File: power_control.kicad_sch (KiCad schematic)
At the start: 21 parts, among them J3 Conn_01x03_Pin, Q1 2N7002, Q2 2N7002, Q3 DTC143Z, SW1 SW_Slide_DPDT, SW2 SW_Push, U4 TPD1E10B06DPYR, U5 TPD1E10B06DPYR

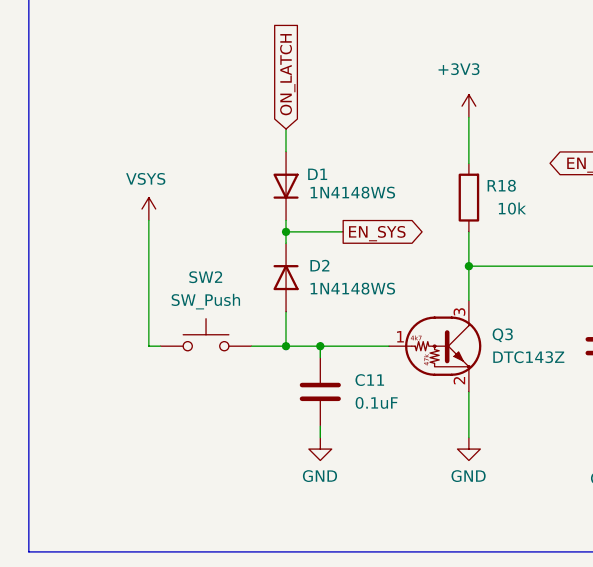
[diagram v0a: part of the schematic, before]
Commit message: v1 Revision - Better routing - Added testpoints - DUCK - Tweaked drawings
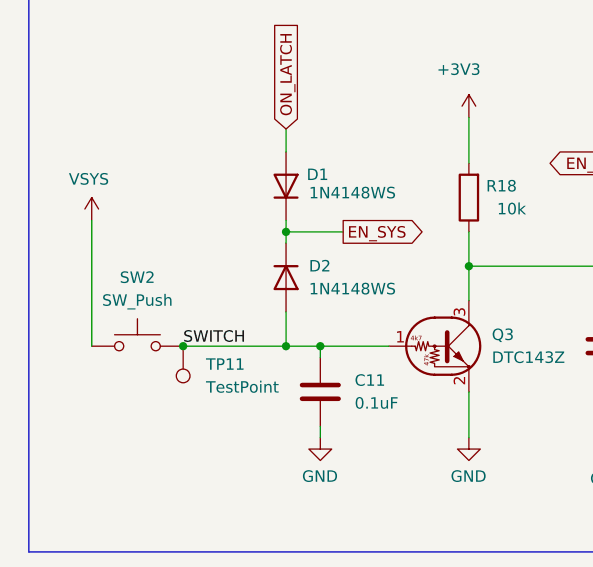
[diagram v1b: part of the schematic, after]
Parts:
- added TP11: TestPoint, TestPoint:TestPoint_Pad_D1.0mm, symbol Connector:TestPoint
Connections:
- net SWITCH: now reaches C11.1, D2.2 (A), Q3.1 (B), SW2.2
- net SWITCH: now also TP11.1
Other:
- moved on the sheet: SW2
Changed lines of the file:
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@@
 	)
 	(junction
+		(at 81.28 144.78)
+		(diameter 0)
+		(color 0 0 0 0)
+	)
+	(junction
 		(at 134.62 124.46)
 		(diameter 0)
@@
 	(wire
 		(pts
-			(xy 88.9 144.78) (xy 92.71 144.78)
+			(xy 81.28 144.78) (xy 92.71 144.78)
 		)
 		(stroke
@@
 	(wire
 		(pts
-			(xy 77.47 130.81) (xy 77.47 144.78)
+			(xy 71.12 130.81) (xy 71.12 144.78)
 		)
 		(stroke
@@
 	(wire
 		(pts
-			(xy 77.47 144.78) (xy 78.74 144.78)
-		)
-		(stroke
-			(width 0)
-			(type default)
-		)
-	)
-	(wire
-		(pts
 			(xy 170.18 86.36) (xy 170.18 88.9)
 		)
@@
 		)
 	)
+	(label "SWITCH"
+		(at 81.28 144.78 0)
+		(effects
+			(font
+				(size 1.27 1.27)
+			)
+			(justify left bottom)
+		)
+	)
 	(global_label "EN_LOAD_BATT"
 		(shape input)
@@
 	)
 	(symbol
+		(lib_id "Connector:TestPoint")
+		(at 81.28 144.78 180)
+		(unit 1)
+		(exclude_from_sim no)
+		(in_bom no)
+		(on_board yes)
+		(dnp no)
+		(fields_autoplaced yes)
+		(property "Reference" "TP11"
+			(at 83.82 146.8119 0)
+			(effects
+				(font
+					(size 1.27 1.27)
+				)
+				(justify right)
+			)
+		)
+		(property "Value" "TestPoint"
+			(at 83.82 149.3519 0)
+			(effects
+				(font
+					(size 1.27 1.27)
+				)
+				(justify right)
+			)
+		)
+		(property "Footprint" "TestPoint:TestPoint_Pad_D1.0mm"
+			(at 76.2 144.78 0)
+			(effects
+				(font
+					(size 1.27 1.27)
+				)
+				(hide yes)
+			)
+		)
+		(property "Datasheet" "~"
+			(at 76.2 144.78 0)
+			(effects
+				(font
+					(size 1.27 1.27)
+				)
+				(hide yes)
+			)
+		)
+		(property "Description" "test point"
+			(at 81.28 144.78 0)
+			(effects
+				(font
+					(size 1.27 1.27)
+				)
+				(hide yes)
+			)
+		)
+		(pin "1"
+		)
+		(instances
+			(project "DRP.004"
+				(path "/990f0ec4-1b5b-4db8-8f39-ecd88fffeea0/6cce2e90-e51c-4942-a042-f4f9f078d271/72eb472c-a375-4523-9048-0cd870109a09"
+					(reference "TP11")
+					(unit 1)
+				)
+			)
+		)
+	)
+	(symbol
 		(lib_id "power:GND")
 		(at 119.38 91.44 0)
@@
 	(symbol
 		(lib_id "power:VCC")
-		(at 77.47 130.81 0)
+		(at 71.12 130.81 0)
 		(mirror y)
 		(unit 1)
@@
 		(dnp no)
 		(property "Reference" "#PWR038"
-			(at 77.47 134.62 0)
+			(at 71.12 134.62 0)
 			(effects
 				(font
@@
 		)
 		(property "Value" "VSYS"
-			(at 74.93 126.238 0)
+			(at 68.58 126.238 0)
 			(effects
 				(font
@@
 		)
 		(property "Footprint" ""
-			(at 77.47 130.81 0)
+			(at 71.12 130.81 0)
 			(effects
 				(font
@@
 		)
 		(property "Datasheet" ""
-			(at 77.47 130.81 0)
+			(at 71.12 130.81 0)
 			(effects
 				(font
@@
 		)
 		(property "Description" "Power symbol creates a global label with name \"VCC\""
-			(at 77.47 130.81 0)
+			(at 71.12 130.81 0)
 			(effects
 				(font
@@
 	(symbol
 		(lib_id "Switch:SW_Push")
-		(at 83.82 144.78 0)
+		(at 76.2 144.78 0)
 		(unit 1)
 		(exclude_from_sim no)
@@
 		(fields_autoplaced yes)
 		(property "Reference" "SW2"
-			(at 83.82 137.16 0)
+			(at 76.2 137.16 0)
 			(effects
 				(font
@@
 		)
 		(property "Value" "SW_Push"
-			(at 83.82 139.7 0)
+			(at 76.2 139.7 0)
 			(effects
 				(font
@@
 		)
 		(property "Footprint" "SWITCHES:SW_SPST_PTS645"
-			(at 83.82 139.7 0)
+			(at 76.2 139.7 0)
 			(effects
 				(font
@@
 		)
 		(property "Datasheet" "~"
-			(at 83.82 139.7 0)
+			(at 76.2 139.7 0)
 			(effects
 				(font
@@
 		)
 		(property "Description" "Push button switch, generic, two pins"
-			(at 83.82 144.78 0)
+			(at 76.2 144.78 0)
 			(effects
 				(font
@@
 		)
 		(property "LCSC" "C2837531"
-			(at 83.82 144.78 0)
+			(at 76.2 144.78 0)
 			(effects
 				(font
@@
 		)
 		(property "lcsc" ""
-			(at 83.82 144.78 0)
+			(at 76.2 144.78 0)
 			(effects
 				(font

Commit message: v2 Rev
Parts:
- removed R14, R15: 100k, Resistor_SMD:R_0603_1608Metric, symbol Device:R
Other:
- moved on the sheet: C15, Q1, R12

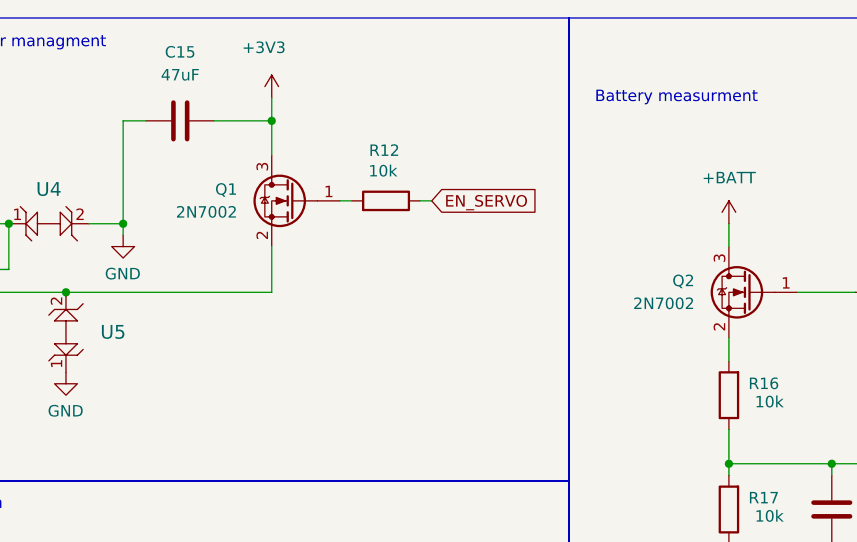
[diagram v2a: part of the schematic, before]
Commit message: Buffed MOSFETs - Changed Q1,Q2 to AO3400 - Changed Q4 to DMG1012T
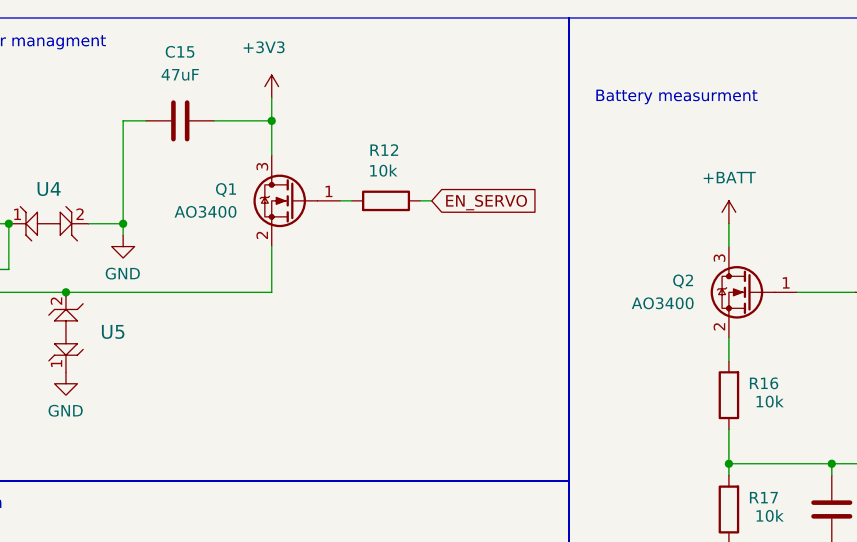
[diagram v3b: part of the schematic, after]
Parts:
- Q1, Q2: value 2N7002 -> AO3400; symbol Transistor_FET:2N7002 -> Transistor_FET:AO3400A; LCSC C8545 -> C4748722
- Q3: LCSC C6423741 -> C2828442
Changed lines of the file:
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@@
 	)
 	(symbol
-		(lib_id "Transistor_FET:2N7002")
+		(lib_id "Transistor_FET:AO3400A")
 		(at 172.72 81.28 0)
 		(mirror y)
@@
 			)
 		)
-		(property "Value" "2N7002"
+		(property "Value" "AO3400"
 			(at 166.37 82.5499 0)
 			(effects
@@
 			)
 		)
-		(property "Datasheet" "https://www.onsemi.com/pub/Collateral/NDS7002A-D.PDF"
+		(property "Datasheet" "http://www.aosmd.com/pdfs/datasheet/AO3400A.pdf"
 			(at 167.64 85.09 0)
 			(effects
@@
 			)
 		)
-		(property "Description" "0.115A Id, 60V Vds, N-Channel MOSFET, SOT-23"
+		(property "Description" "30V Vds, 5.7A Id, N-Channel MOSFET, SOT-23"
 			(at 172.72 81.28 0)
 			(effects
@@
 			)
 		)
-		(property "LCSC" "C8545"
+		(property "LCSC" "C4748722"
 			(at 172.72 81.28 0)
 			(effects
@@
 			)
 		)
-		(property "LCSC" "C6423741"
+		(property "LCSC" "C2828442"
 			(at 110.49 144.78 0)
 			(effects
@@
 	)
 	(symbol
-		(lib_id "Transistor_FET:2N7002")
+		(lib_id "Transistor_FET:AO3400A")
 		(at 121.92 71.12 0)
 		(mirror y)
@@
 			)
 		)
-		(property "Value" "2N7002"
+		(property "Value" "AO3400"
 			(at 115.57 72.3899 0)
 			(effects
@@
 			)
 		)
-		(property "Datasheet" "https://www.onsemi.com/pub/Collateral/NDS7002A-D.PDF"
+		(property "Datasheet" "http://www.aosmd.com/pdfs/datasheet/AO3400A.pdf"
 			(at 116.84 74.93 0)
 			(effects
@@
 			)
 		)
-		(property "Description" "0.115A Id, 60V Vds, N-Channel MOSFET, SOT-23"
+		(property "Description" "30V Vds, 5.7A Id, N-Channel MOSFET, SOT-23"
 			(at 121.92 71.12 0)
 			(effects
@@
 			)
 		)
-		(property "LCSC" "C8545"
+		(property "LCSC" "C4748722"
 			(at 121.92 71.12 90)
 			(effects

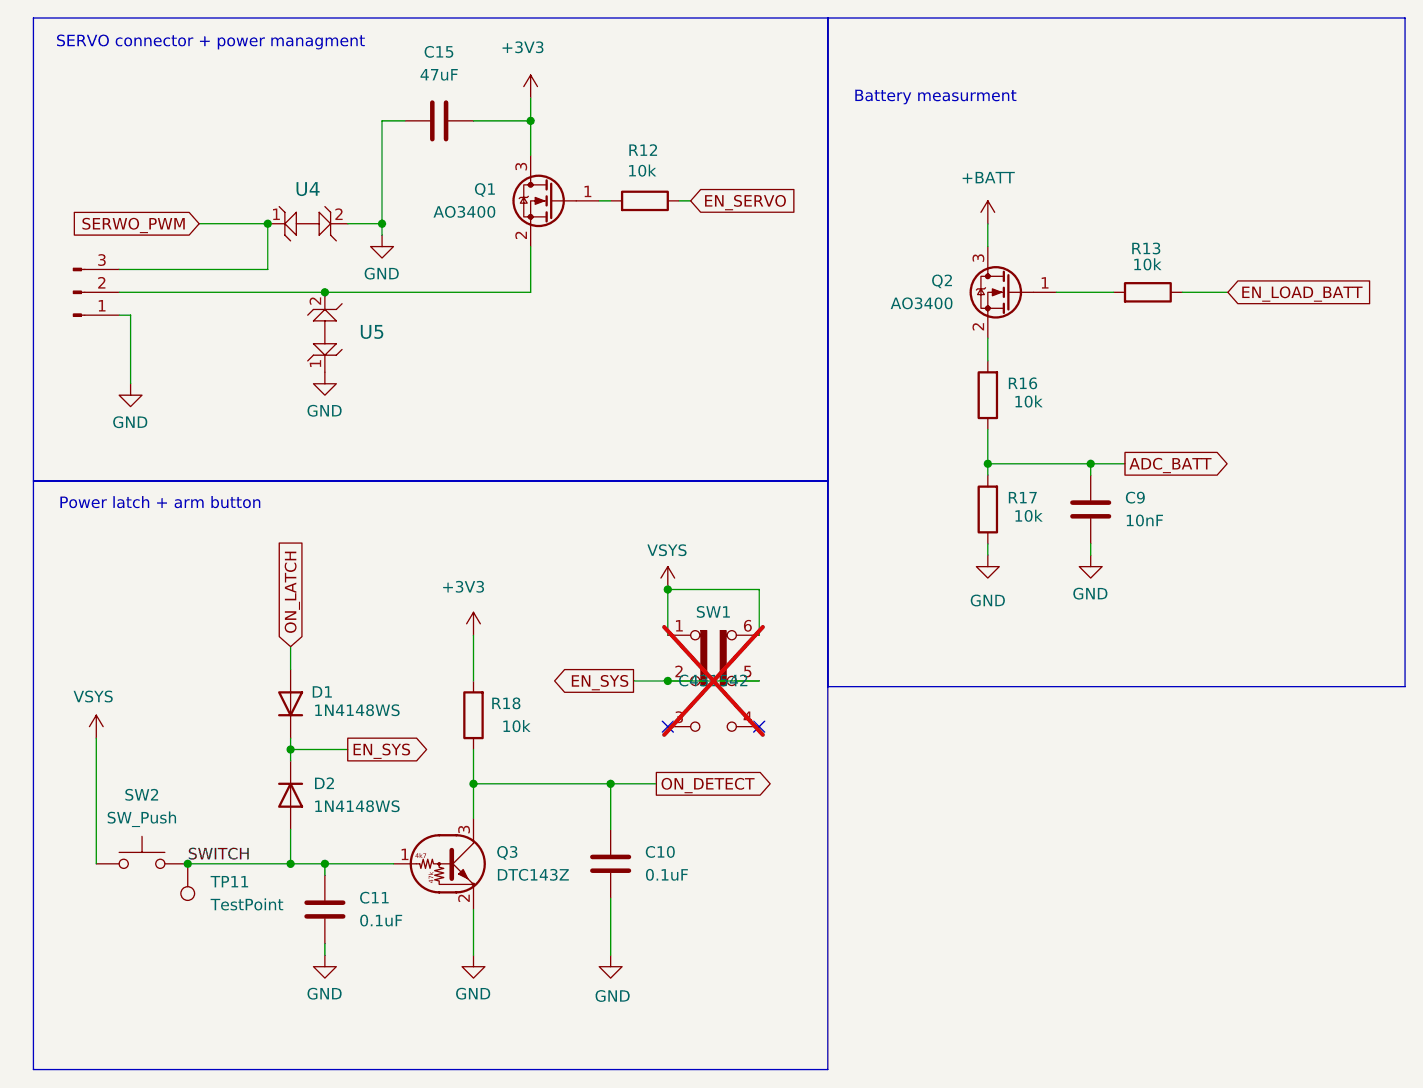
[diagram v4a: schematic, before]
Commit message: Rough placment of components for v3
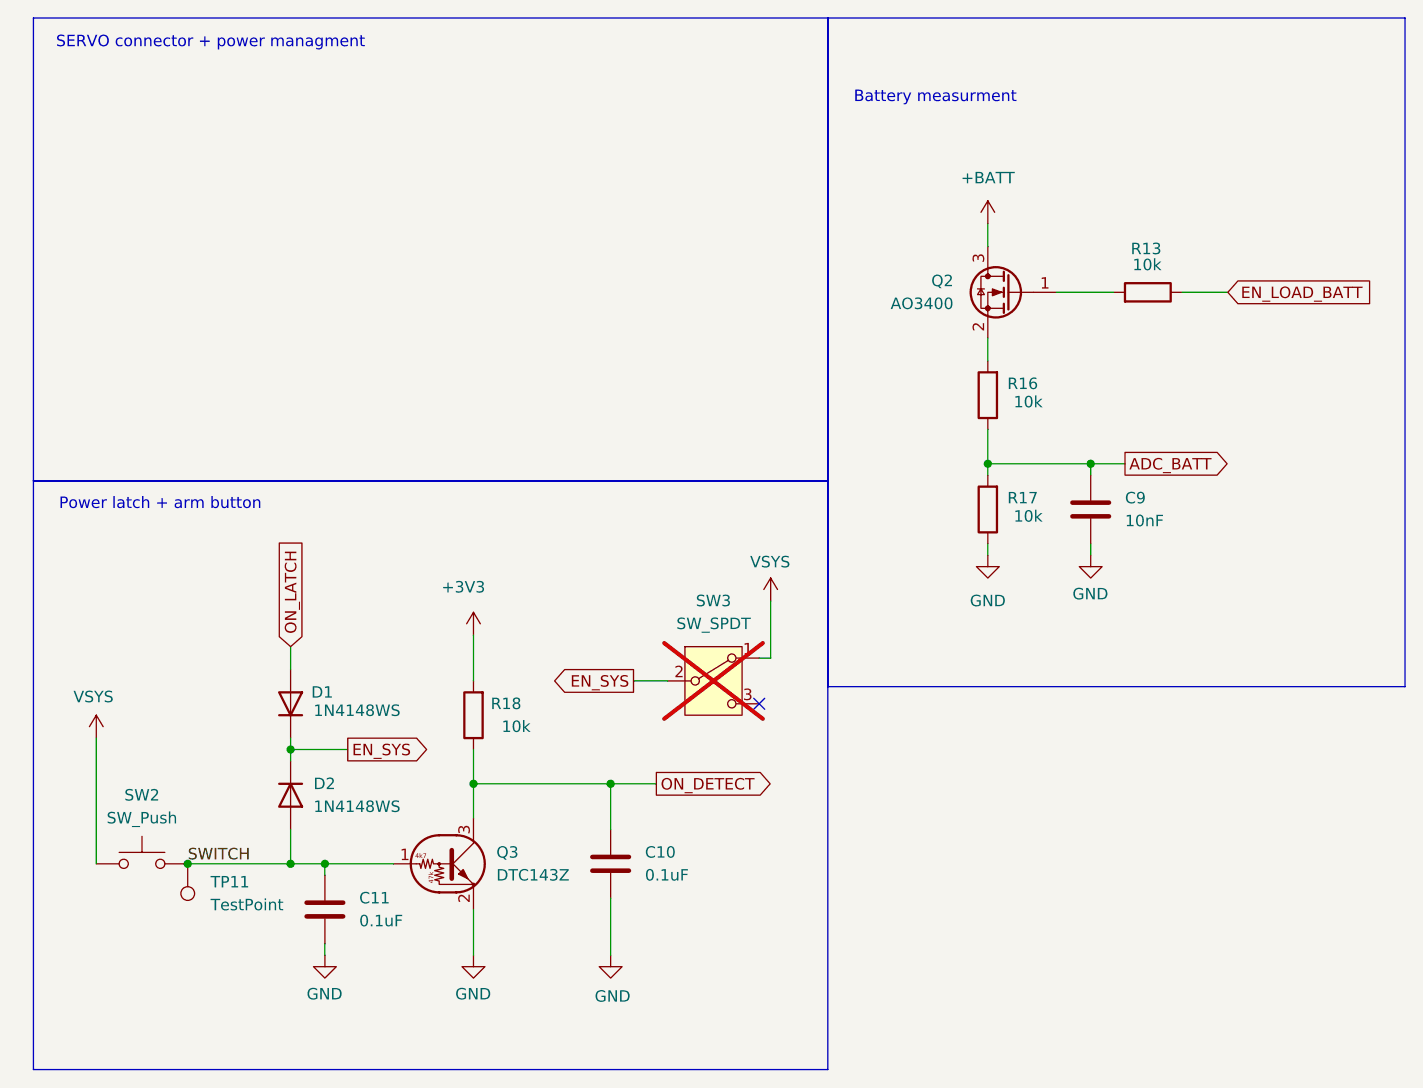
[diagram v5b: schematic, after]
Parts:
- removed C15: 47uF, Capacitor_SMD:C_1206_3216Metric, symbol Device:C
- removed J3: Conn_01x03_Pin, conn:PinHeader_1x03_P2.54mm_Horizontal, symbol Connector:Conn_01x03_Pin
- removed Q1: AO3400, Package_TO_SOT_SMD:SOT-23, symbol Transistor_FET:AO3400A
- removed R12: 10k, Resistor_SMD:R_0603_1608Metric, symbol Device:R
- removed SW1: SW_Slide_DPDT, Button_Switch_THT:SW_CK_JS202011CQN_DPDT_Straight, symbol Switch:SW_Slide_DPDT
- removed U4, U5: TPD1E10B06DPYR, TPD1E10B06DPYR:X1SON-2_L1.0-W0.6-P0.65-BI, symbol TPD1E10B06DPYR:TPD1E10B06DPYR
- added SW3: SW_SPDT, Button_Switch_THT:SW_Slide_SPDT_Angled_CK_OS102011MA1Q, symbol Switch:SW_SPDT
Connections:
- net EN_SYS: now also SW3.2 (B)
- net VSYS: now also SW3.1 (A)
- no-connect marks 2 -> 1
